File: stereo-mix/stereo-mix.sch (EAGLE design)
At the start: 22 parts, among them IC3 LM324N

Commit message: gerber
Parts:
- removed C10, C9: 4.7u, rcl:CPOL-USA
- removed D3, D4: 1N5819HW, diode:1N5819-B
- removed JP2: M05X2PTH, og-header:M05X2PTH
- removed RIGHT1: THONKICONNNEW, MusicThingModular:THONKICONNNEW
- added D1, D2: 1N5819-B, diode:1N5819-B
- added R1, R2: 1k, MusicThingModular:RESISTOR7MM
- added R10, R3, R4, R7, R8, R9: 100k, MusicThingModular:RESISTOR7MM
- added SV1: EURO_POWER_HEADERREGULAR, MusicThingModular:EURO_POWER_HEADERREGULAR
- added U4: THONKICONNNEW, MusicThingModular:THONKICONNNEW
- R5, R6: value 1k -> 100k; device MusicThingModular:RESISTOR10MM_RESISTOR -> MusicThingModular:RESISTOR7MM
- renumbered GAIN1 to VR1, GAIN2 to VR2, GAIN3 to VR3, GAIN4 to VR4, IC3 to IC1, LEFT1 to U2, LEFT2 to U5, LEFT3 to U7, LEFT4 to U9, RIGHT2 to U6, RIGHT3 to U8, RIGHT4 to U10, SUM_LEFT to U1, SUM_RIGHT to U3
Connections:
- removed net N$23: D4.A, JP2.1, JP2.2
- removed net N$24: D3.C, JP2.10, JP2.9
- removed net N$26: RIGHT1.TIP, U2.SWITCH
- removed net N$30: RIGHT1.SWITCH, VR1G$2.E
- removed net N$34: U5.SWITCH, U6.TIP
- removed net N$35: U5.TIP, VR2G$1.E
- removed net N$36: U6.SWITCH, VR2G$2.E
- removed net N$39: U7.SWITCH, U8.TIP
- removed net N$41: U8.SWITCH, VR3G$2.E
- removed net N$44: U10.TIP, U9.SWITCH
- removed net N$46: U10.SWITCH, VR4G$2.E
- new net N$1: R4.2, VR1G$2.S
- new net N$10: D2.C, SV1.2
- new net N$11: U4.TIP, VR1G$2.E
- new net N$12: U5.TIP, U6.SWITCH, VR2G$1.E
- new net N$13: U6.TIP, VR2G$2.E
- new net N$14: D1.A, SV1.10
- new net N$15: U8.TIP, VR3G$2.E
- new net N$18: U10.TIP, VR4G$2.E
- new net N$2: R3.2, VR1G$1.S
- new net N$3: R5.2, VR2G$1.S
- new net N$4: R6.2, VR2G$2.S
- new net N$5: R7.2, VR3G$1.S
- new net N$7: R8.2, VR3G$2.S
- new net N$8: R9.2, VR4G$1.S
- new net N$9: R10.2, VR4G$2.S
- net GND: now also SV1.3, SV1.5, SV1.7, U4.SLEEVE, VR1G$1.A, VR1G$2.A, VR2G$1.A, VR2G$2.A, VR3G$1.A, VR3G$2.A, VR4G$1.A, VR4G$2.A; no longer C10.+, C9.-, JP2.3, JP2.4, JP2.5, JP2.6, JP2.7, JP2.8, RIGHT1.SLEEVE
- net N$20: now also R2.1; no longer R6.1
- net N$25: now also U4.SWITCH
- net N$27: now also R2.2; no longer R6.2
- net N$29: now also R1.2; no longer R5.2
- net N$40: now also U8.SWITCH
- net N$45: now also U10.SWITCH
- net N$47: now also R3.1, R5.1, R7.1, R9.1; no longer VR1G$1.S, VR2G$1.S, VR3G$1.S, VR4G$1.S
- net N$48: now also R10.1, R4.1, R6.1, R8.1; no longer VR1G$2.S, VR2G$2.S, VR3G$2.S, VR4G$2.S
- net N$6: now also R1.1; no longer R5.1
- net VCC: now also D1.C; no longer C9.+, D4.C
- net VEE: now also D2.A; no longer C10.-, D3.A
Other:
- note removed: "EEE-1EA100WR"
- moved on the sheet: R5, R6

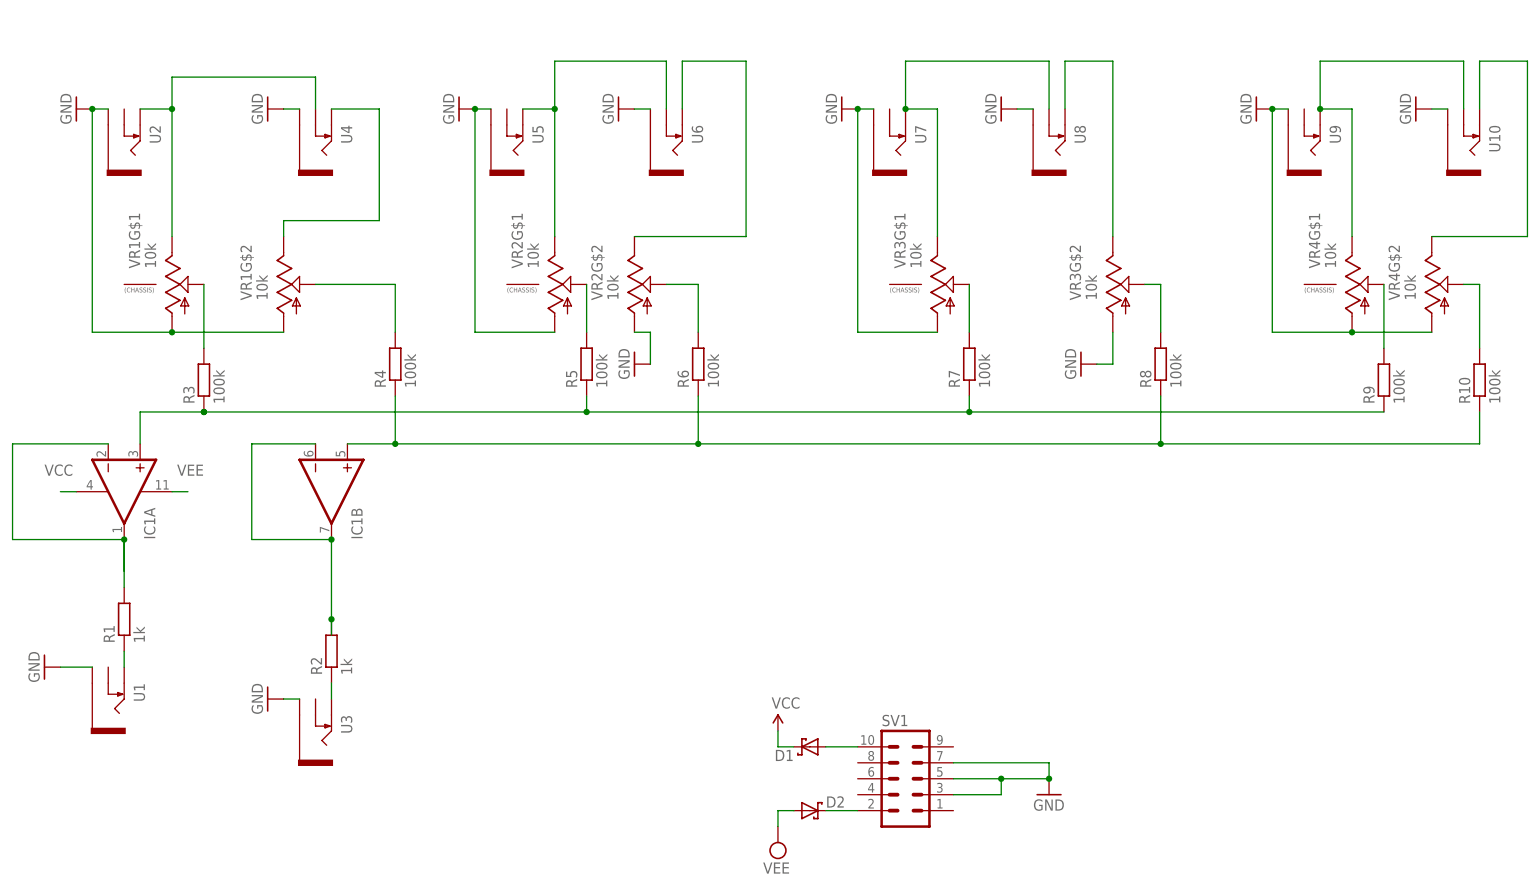
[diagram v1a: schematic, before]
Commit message: update stereo-mix 0.0.2
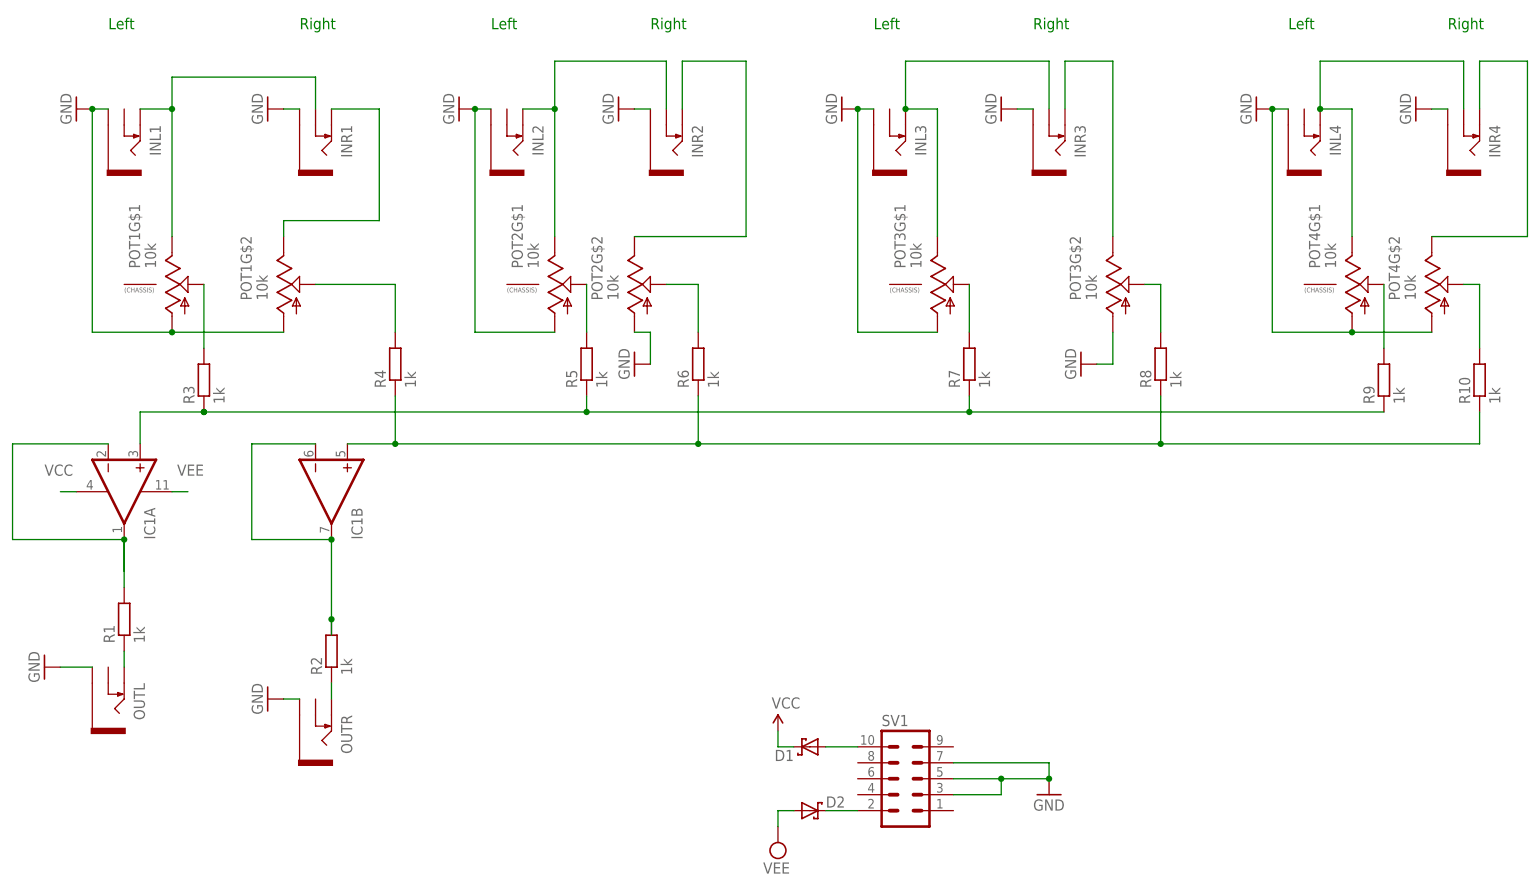
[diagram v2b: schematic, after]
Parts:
- R10, R3, R4, R5, R6, R7, R8, R9: value 100k -> 1k
- renumbered U1 to OUTL, U10 to INR4, U2 to INL1, U3 to OUTR, U4 to INR1, U5 to INL2, U6 to INR2, U7 to INL3, U8 to INR3, U9 to INL4, VR1 to POT1, VR2 to POT2, VR3 to POT3, VR4 to POT4
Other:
- note added: "Left"
- note added: "Right"
